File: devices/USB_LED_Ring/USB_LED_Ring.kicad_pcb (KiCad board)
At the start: 2 copper layers, 91.6 x 75.1 mm, 84 parts, among them J1 JST SH 3 Vert, J2 USB_B_Micro, J3 JST SH 3 Vert, J4 .100, Q1 DMG2305UX, U1 TPS923610, U2 TLV75733PDBV, U3 RP2354A, Y1 ABM8-272-T3

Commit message: Improves the input filter of the LED driver (no self-excitation)
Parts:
- removed kibuzzard-6A0471EB: G***, kibuzzard-6A0471EB
- added kibuzzard-6A11720E: G***, kibuzzard-6A11720E, F.Cu at (196.4, 90.9)
- added kibuzzard-6A117223: G***, kibuzzard-6A117223, F.Cu at (201.5, 89.8)
- added kibuzzard-6A11723A: G***, kibuzzard-6A11723A, F.Cu at (197.9, 84.7)
- FB1: value MPZ1608S601A -> MLZ2012DR22DT000; footprint Inductor_SMD:L_0603_1608Metric -> Inductor_SMD:L_0805_2012Metric
- moved TP4 4.73 mm to (197.9, 86.3), turned to 90 degrees
- moved TP5 2.65 mm to (199.7, 89.8)
- moved kibuzzard-69FB66A2 2.51 mm to (183.3, 94.3)
- moved kibuzzard-69FB6681 2.48 mm to (183.6, 96.6)
- moved Q1 1.86 mm to (195.6, 86.5)
- moved R2 0.67 mm to (197.9, 88.9), turned to -90 degrees
- moved C7 0.65 mm to (198.3, 92.6)
- moved Y1 0.65 mm to (200.6, 93.5)
- moved C6 0.65 mm to (198.3, 94.5)
- moved R3 0.65 mm to (196.4, 93.1)
- moved FB1 0.11 mm to (195.3, 89.3)
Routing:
- net /XIN: track 9.62 -> 10.6 mm
- net /XOUT: track 4.82 -> 5.68 mm
- net Net-(FB1-Pad2): track 2.90 -> 3.54 mm
- net GND: vias 30 -> 39

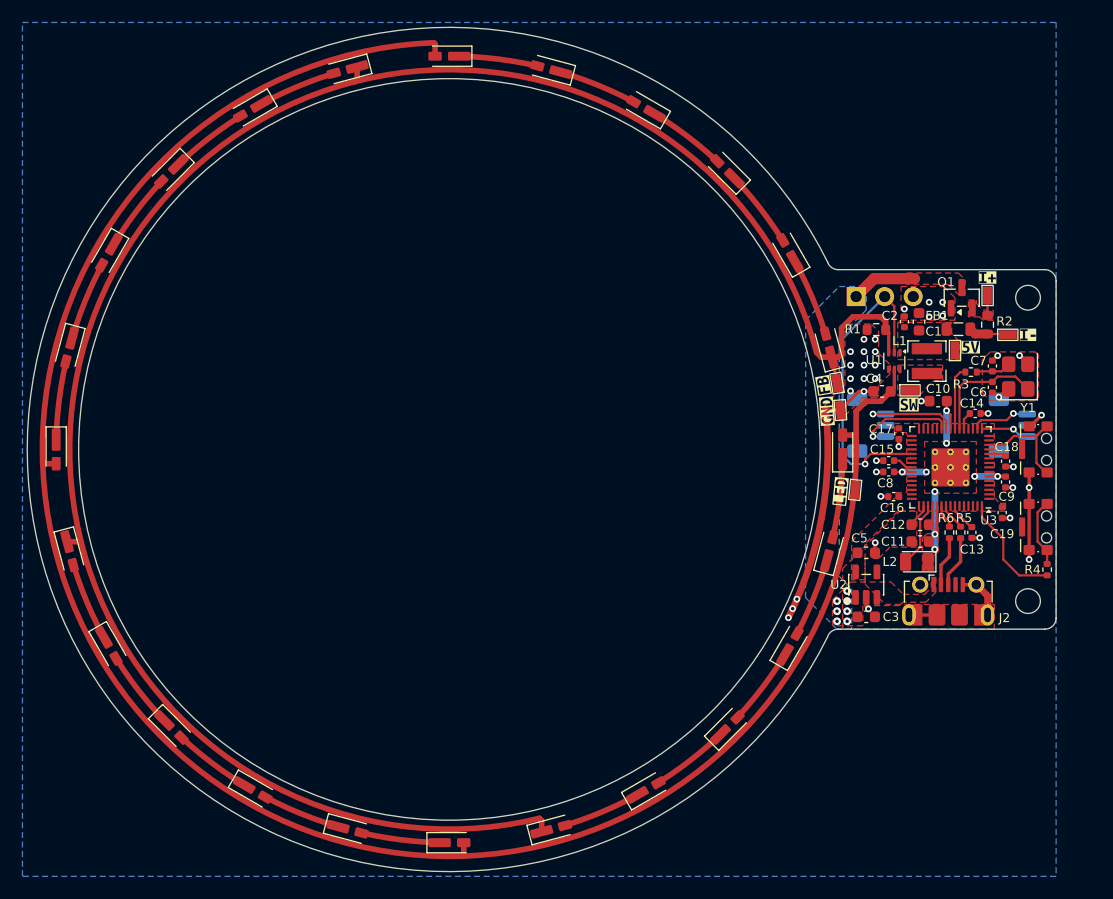
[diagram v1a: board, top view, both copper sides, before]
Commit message: Improves input filter for LED driver
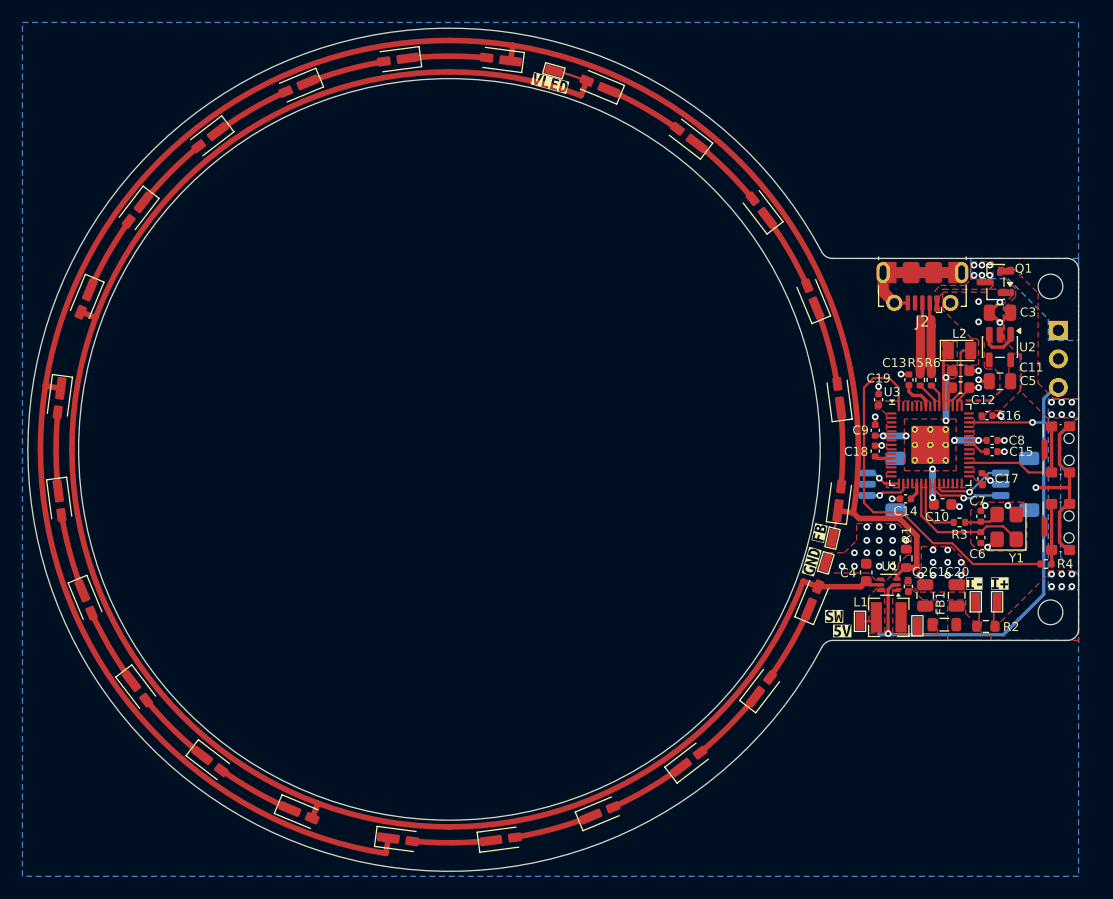
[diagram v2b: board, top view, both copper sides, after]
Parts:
- removed kibuzzard-69FB6681: G***, kibuzzard-69FB6681
- removed kibuzzard-69FB66A2: G***, kibuzzard-69FB66A2
- removed kibuzzard-69FB66BC: G***, kibuzzard-69FB66BC
- removed kibuzzard-69FC8383: G***, kibuzzard-69FC8383
- removed kibuzzard-6A01CBA8: G***, kibuzzard-6A01CBA8
- removed kibuzzard-6A11720E: G***, kibuzzard-6A11720E
- added C20: 2u2, Capacitor_SMD:C_0805_2012Metric, F.Cu at (195.2, 113.0)
- added kibuzzard-6A15B584: G***, kibuzzard-6A15B584, F.Cu at (184.3, 114.9)
- added kibuzzard-6A15B5C8: G***, kibuzzard-6A15B5C8, F.Cu at (182.2, 110.0)
- added kibuzzard-6A15B5E0: G***, kibuzzard-6A15B5E0, F.Cu at (182.9, 107.4)
- added kibuzzard-6A15B60A: G***, kibuzzard-6A15B60A, F.Cu at (159.0, 67.4)
- added kibuzzard-6A15B62E: G***, kibuzzard-6A15B62E, F.Cu at (185.0, 116.2)
- added kibuzzard-6A15B6D3: G***, kibuzzard-6A15B6D3, B.Cu at (203.4, 102.9)
- C1, C3, C5: footprint Capacitor_SMD:C_0603_1608Metric -> Capacitor_SMD:C_0805_2012Metric
- J2: footprint Connector_USB:USB_Micro-B_Molex-105017-0001 -> custom:USB_Micro-B_Molex-105017-0001
- R2: value 250m -> 150m
- moved TP2 45.9 mm to (159.3, 66.3), turned to -15.42 degrees
- moved C3 29.6 mm to (199.0, 87.8), turned to 180 degrees
- moved J2 28.1 mm to (192.1, 85.5), turned to 180 degrees
- moved TP4 27.3 mm to (198.8, 113.6)
- moved kibuzzard-6A11723A 27.3 mm to (199.0, 111.9)
- moved R2 26.9 mm to (197.8, 115.8), turned to 180 degrees
- moved FB1 26.3 mm to (194.1, 115.6)
- moved TP7 24.7 mm to (191.7, 115.7)
- moved C1 24.4 mm to (192.3, 113.0)
- moved U2 24.3 mm to (199.0, 90.9), turned to -90 degrees
- moved TP5 23.9 mm to (196.8, 113.6), turned to 90 degrees
- moved C2 23.6 mm to (190.8, 112.2)
- moved L1 23.1 mm to (189.1, 115.0), turned to 180 degrees
- moved kibuzzard-6A117223 22.6 mm to (196.7, 111.9)
- moved TP1 21.0 mm to (186.6, 115.3), turned to 90 degrees
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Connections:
- net /QSPI_SS renamed /BTSEL
- net Net-(FB1-Pad2) renamed /SNS
- BTN1 pad 1: GND -> /BTSLB
- BTN1 pad 2: /BTSL -> GND
- BTN2 pad 1: GND -> /BTN
- BTN2 pad 2: /BTN -> GND
- C3 pad 1: VBUS -> VIN
- J4 pad 2: /LED_PWM -> GND
- J4 pad 3: GND -> /LED_PWM
- Q1 pad 2: Net-(Q1-S) -> VIN
- R2 pad 1: Net-(Q1-S) -> VIN
- R4 pad 1: /BTSL -> /BTSLB
- TP4 pad 1: Net-(Q1-S) -> VIN
- U2 pad 1: VBUS -> VIN
- U2 pad 3: VBUS -> VIN
- U3 pad 13: /BTN -> unconnected-(U3-GPIO9-Pad13)
- U3 pad 34: unconnected-(U3-GPIO22-Pad34) -> /BTN
- U3 pad 35: /LED_PWM -> unconnected-(U3-GPIO23-Pad35)
- U3 pad 43: unconnected-(U3-GPIO29_ADC3-Pad43) -> /LED_PWM
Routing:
- net /BTSEL: track 10.0 -> 33.7 mm
- net /LED_PWM: track 28.1 -> 46.9 mm, vias 1 -> 2
- net GND: track 35.4 -> 44.2 mm, vias 39 -> 45
- net /VLED: track 12.9 -> 5.88 mm
- net /BTSL: track 6.17 -> 0.00 mm
- net VIN: track 0.00 -> 6.03 mm, vias 0 -> 12
- net VBUS: track 5.86 -> 0.00 mm, vias 7 -> 6
- net /BTSLB: track 0.00 -> 5.35 mm
- net /LED_FB: track 16.1 -> 11.6 mm
- net /D-: track 4.45 -> 6.98 mm
- net /BTN: track 9.70 -> 11.8 mm
- net /SWDIO: track 8.88 -> 6.77 mm
- net /XIN: track 10.6 -> 12.6 mm
- net /D+: track 4.59 -> 6.42 mm
- net Net-(Q1-S): track 1.78 -> 0.00 mm
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- added copper zone on F.Cu, net /SNS
- added copper zone on B.Cu, net VIN
- added copper zone on F.Cu, net VIN
- removed copper zone on F.Cu, net Net-(Q1-S)
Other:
- board size 91.6 x 75.1 mm -> 93.5 x 75 mm

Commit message: !fixup
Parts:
- removed FB1: MLZ2012DR22DT000, Inductor_SMD:L_0805_2012Metric
- removed Q1: DMG2305UX, Package_TO_SOT_SMD:SOT-23
- removed TP7: RCUCTE, custom:RCUCTE
- removed kibuzzard-6A15B62E: G***, kibuzzard-6A15B62E
- added C21: 1n, Capacitor_SMD:C_0402_1005Metric, F.Cu at (190.6, 115.7)
- added L3: 220n, LED_SMD:LED_0805_2012Metric, F.Cu at (188.1, 91.0)
- added R10: 130k, Resistor_SMD:R_0402_1005Metric, F.Cu at (192.3, 111.9)
- added R11: 47k, Resistor_SMD:R_0402_1005Metric, F.Cu at (190.9, 112.4)
- added R7: 6k8, Resistor_SMD:R_0402_1005Metric, F.Cu at (192.3, 116.1)
- added R8: 430k, Resistor_SMD:R_0402_1005Metric, F.Cu at (194.8, 111.5)
- added R9: 47k, Resistor_SMD:R_0402_1005Metric, F.Cu at (193.3, 111.9)
- added U4: TPS25947xx, custom:Texas_RPW_VQFN-HR-10_2.1x2.1mm_P0.475mm, F.Cu at (192.3, 114.3)
- C20: value 2u2 -> 4u7
- R2: value 150m -> 100m
- moved kibuzzard-6A15B584 31.0 mm to (186.3, 83.9)
- moved TP1 29.8 mm to (186.3, 85.5)
- moved J2 29.7 mm to (198.4, 114.5), turned to 0 degrees
- moved L1 28.0 mm to (188.8, 86.9), turned to 90 degrees
- moved C4 26.8 mm to (192.8, 84.8), turned to 0 degrees
- moved U1 25.4 mm to (191.7, 86.8), turned to 90 degrees
- moved J4 24.9 mm to (205.2, 114.2), turned to 0 degrees
- moved kibuzzard-69FB6775 24.7 mm to (202.6, 114.1)
- moved C3 24.6 mm to (189.9, 110.7), turned to 0 degrees
- moved C2 23.7 mm to (191.5, 88.5), turned to 0 degrees
- moved R2 23.4 mm to (187.9, 94.5), turned to 90 degrees
- moved C1 23.0 mm to (190.8, 90.0), turned to 0 degrees
- moved kibuzzard-6A15B5C8 22.8 mm to (183.9, 87.2), turned to -69.27 degrees
- moved kibuzzard-6A15B60A 22.6 mm to (136.3, 66.5), turned to 22.08 degrees
- moved D12 22.5 mm to (167.5, 130.3), turned to -150 degrees
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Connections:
- U2 pad 3: VIN -> /RUN
- U3 pad 13: unconnected-(U3-GPIO9-Pad13) -> /BTN
- U3 pad 16: /UART_TX -> unconnected-(U3-GPIO12-Pad16)
- U3 pad 17: /UART_RX -> unconnected-(U3-GPIO13-Pad17)
- U3 pad 2: unconnected-(U3-GPIO0-Pad2) -> /UART_TX
- U3 pad 3: unconnected-(U3-GPIO1-Pad3) -> /UART_RX
- U3 pad 34: /BTN -> /LED_PWM
- U3 pad 43: /LED_PWM -> unconnected-(U3-GPIO29_ADC3-Pad43)
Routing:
- net /LED_PWM: track 46.9 -> 75.1 mm, vias 2 -> 1
- net /BTSEL: track 33.7 -> 20.9 mm, vias 0 -> 2
- net /LED_FB: track 11.6 -> 23.7 mm
- net /VLED: track 5.88 -> 14.8 mm
- net /RUN: track 0.00 -> 8.39 mm, vias 0 -> 2
- net GND: track 44.2 -> 38.9 mm
- net /BTN: track 11.8 -> 7.82 mm
- net /XIN: track 12.6 -> 9.53 mm
- net VBUS: track 0.00 -> 2.80 mm, vias 6 -> 0
- net /UART_TX: track 3.21 -> 5.85 mm
- net /OVLO: track 0.00 -> 2.50 mm
- net /UVLO: track 0.00 -> 2.48 mm
- net /SWDIO: track 6.77 -> 5.63 mm
- net /ILIM: track 0.00 -> 1.02 mm
- net /SW: track 1.59 -> 2.57 mm
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- removed copper zone on B.Cu, net VBUS
- removed copper zone on B.Cu, net VIN
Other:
- board size 93.5 x 75 mm -> 94.5 x 75 mm
